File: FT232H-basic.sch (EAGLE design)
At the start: 27 parts, among them IC1 FT232H

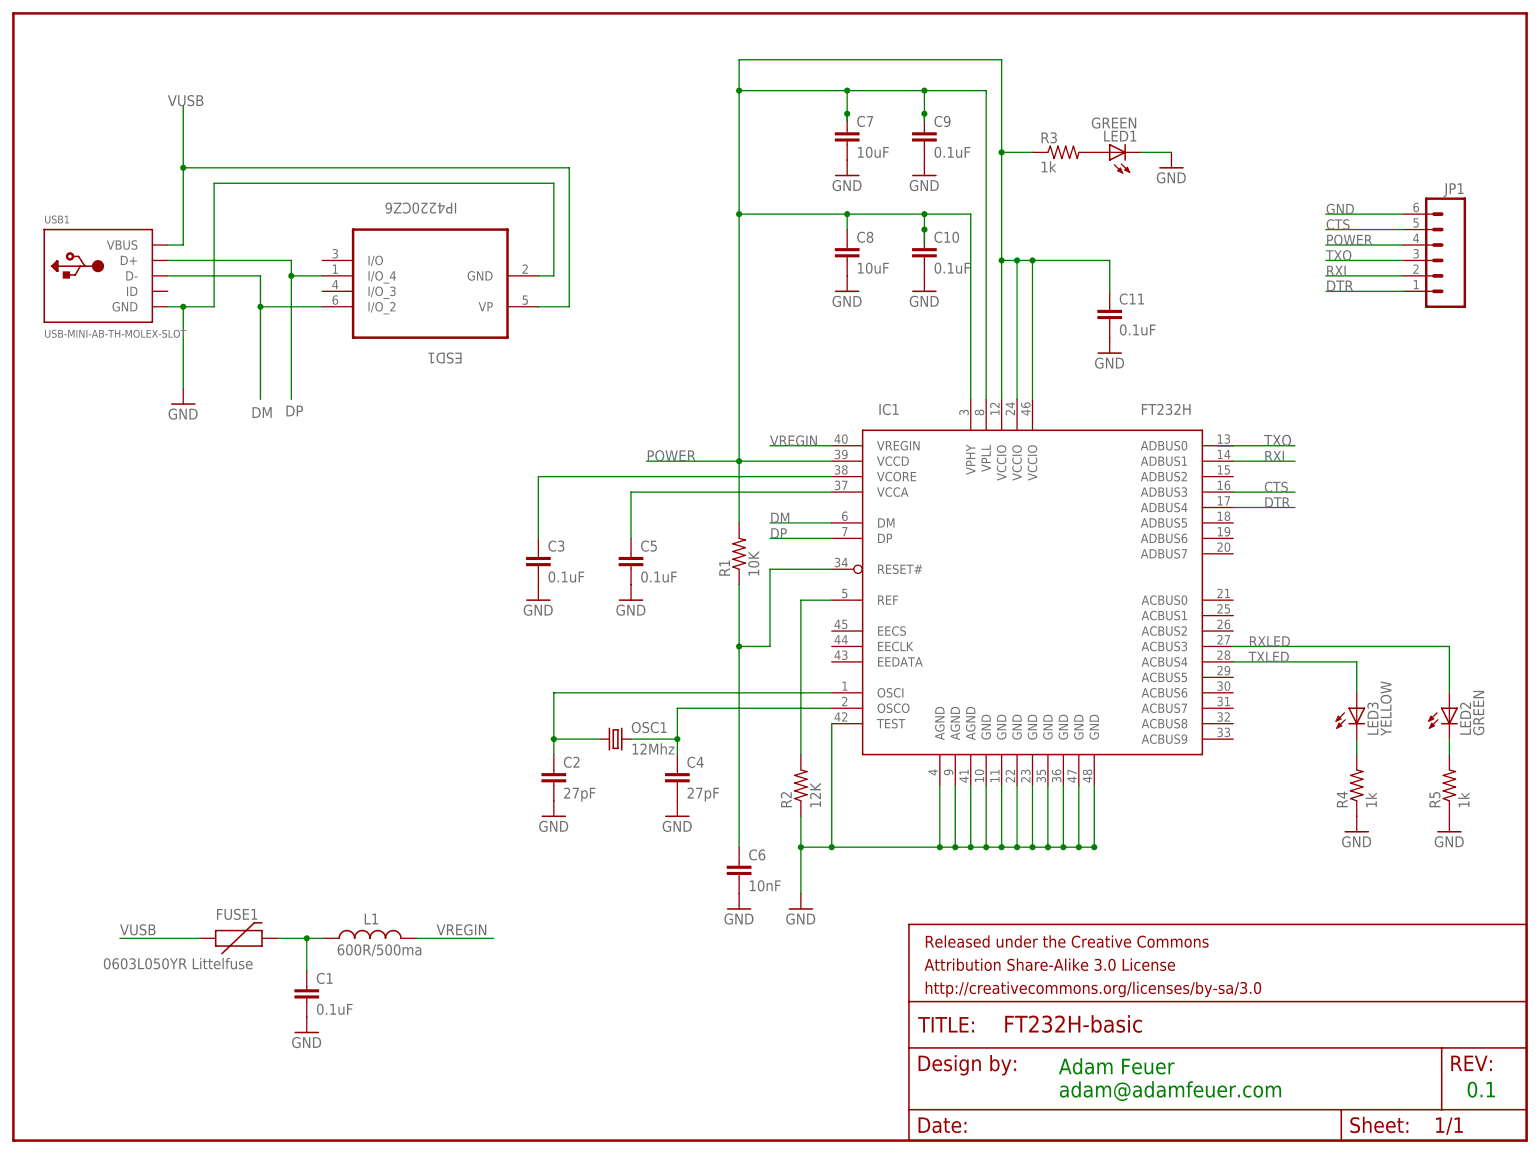
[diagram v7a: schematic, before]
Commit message: moved OSC1 traces so they are not serpentine
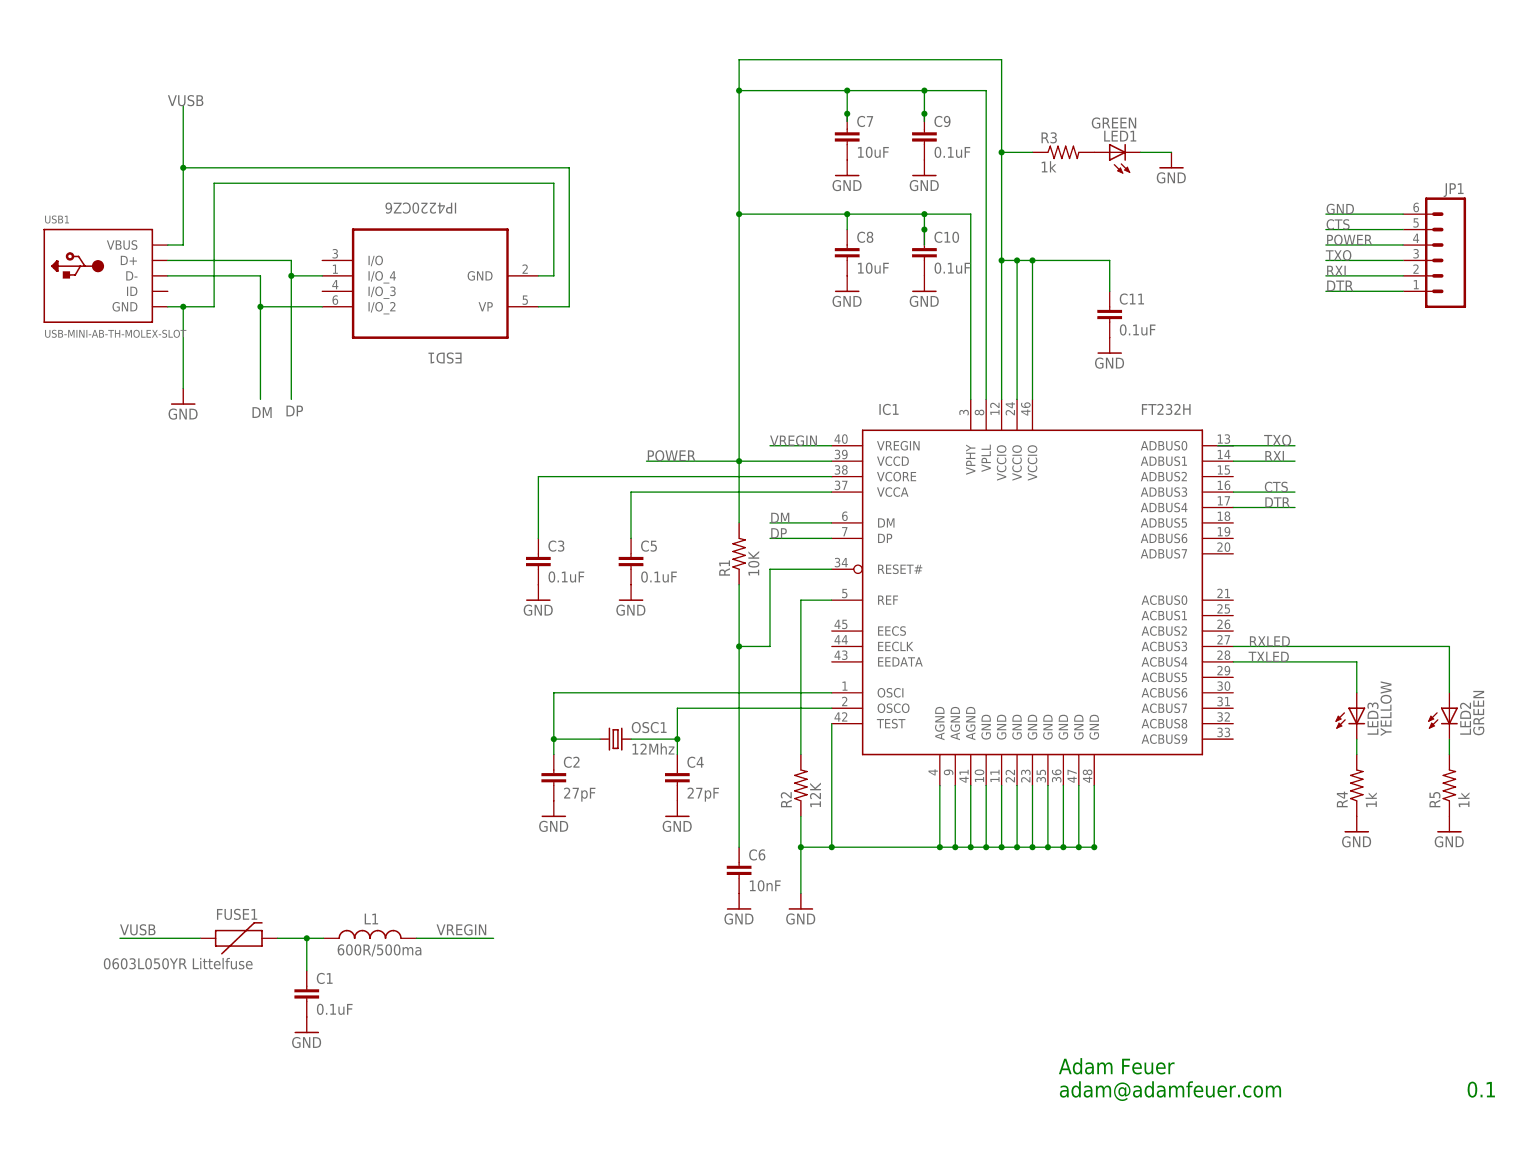
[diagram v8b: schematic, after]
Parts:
- removed FRAME1: FRAME-LETTER, SparkFun-Aesthetics:FRAME-LETTER
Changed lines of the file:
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@@
 <part name="LED1" library="SparkFun-LED" deviceset="LED-GREEN" device="0603" value="GREEN"/>
 <part name="OSC1" library="SparkFun-FreqCtrl" deviceset="CRYSTAL" device="5X3" value="12Mhz"/>
-<part name="FRAME1" library="SparkFun-Aesthetics" deviceset="FRAME-LETTER" device=""/>
 <part name="ESD1" library="NXP_By_element14_Batch_1" deviceset="IP4220CZ6" device=""/>
 <part name="JP1" library="SparkFun-Connectors" deviceset="M06" device="SIP"/>
@@
 <instance part="LED1" gate="G$1" x="180.34" y="162.56" rot="R90"/>
 <instance part="OSC1" gate="G$1" x="99.06" y="66.04"/>
-<instance part="FRAME1" gate="G$1" x="0" y="0"/>
-<instance part="FRAME1" gate="G$2" x="147.32" y="0"/>
 <instance part="ESD1" gate="A" x="68.58" y="137.16" smashed="yes" rot="R180">
 <attribute name="NAME" x="73.9394" y="129.6162" size="1.778" layer="95" rot="SR180"/>
